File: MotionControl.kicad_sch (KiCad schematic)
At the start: 18 parts, among them J2 Conn_ARM_JTAG_SWD_10, Q1 2N7002, SW1 SW_Push, U1 ATSAMD21J18A-A, Y1 32.768kHz

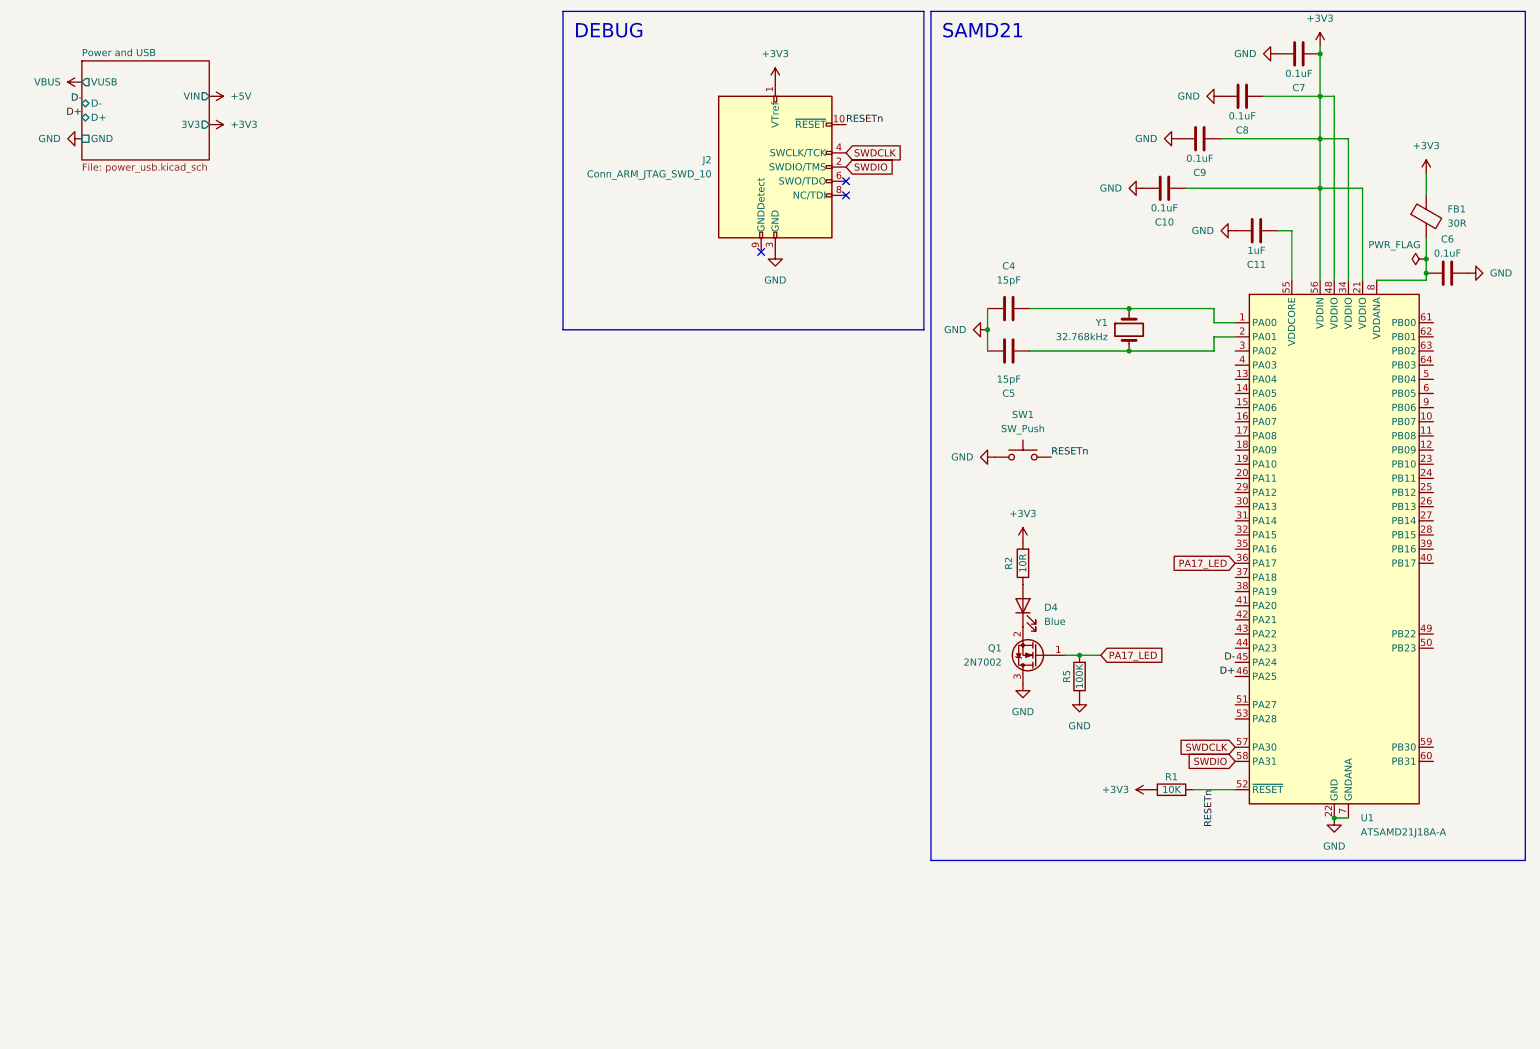
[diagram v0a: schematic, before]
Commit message: tx, rx leds
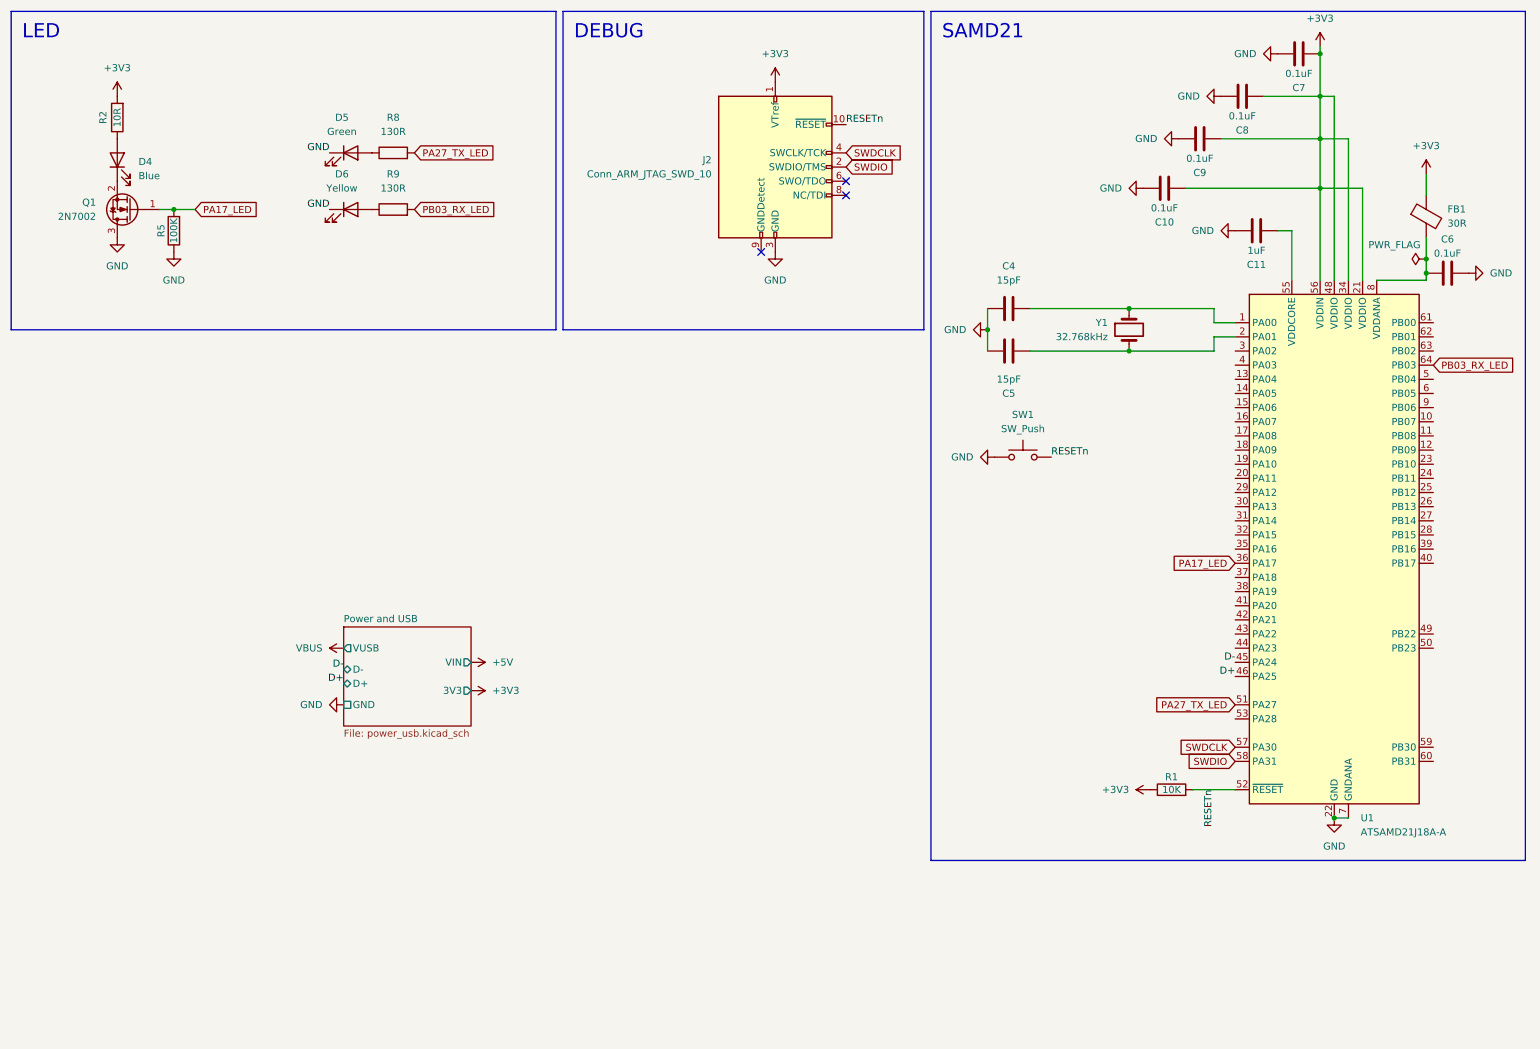
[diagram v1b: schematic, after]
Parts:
- added D5: Green, LED_SMD:LED_0603_1608Metric, symbol Device:LED
- added D6: Yellow, LED_SMD:LED_0603_1608Metric, symbol Device:LED
- added R8, R9: 130R, Resistor_SMD:R_0402_1005Metric, symbol Device:R
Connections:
- net GND: now also D5.1 (K), D6.1 (K)
- net PA27_TX_LED: now reaches U1.51 (PA27)
- net PA27_TX_LED: now also R8.2
- net PB03_RX_LED: now reaches U1.64 (PB03)
- net PB03_RX_LED: now also R9.2
- new net: D6.2 (A), R9.1
- new net: D5.2 (A), R8.1
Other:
- moved on the sheet: D4, Q1, R2, R5

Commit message: Stepper unit
Made first revision for stepper unit
Contains TMC5160, Status LED, FETs, and complementary comps
Will be x4 later
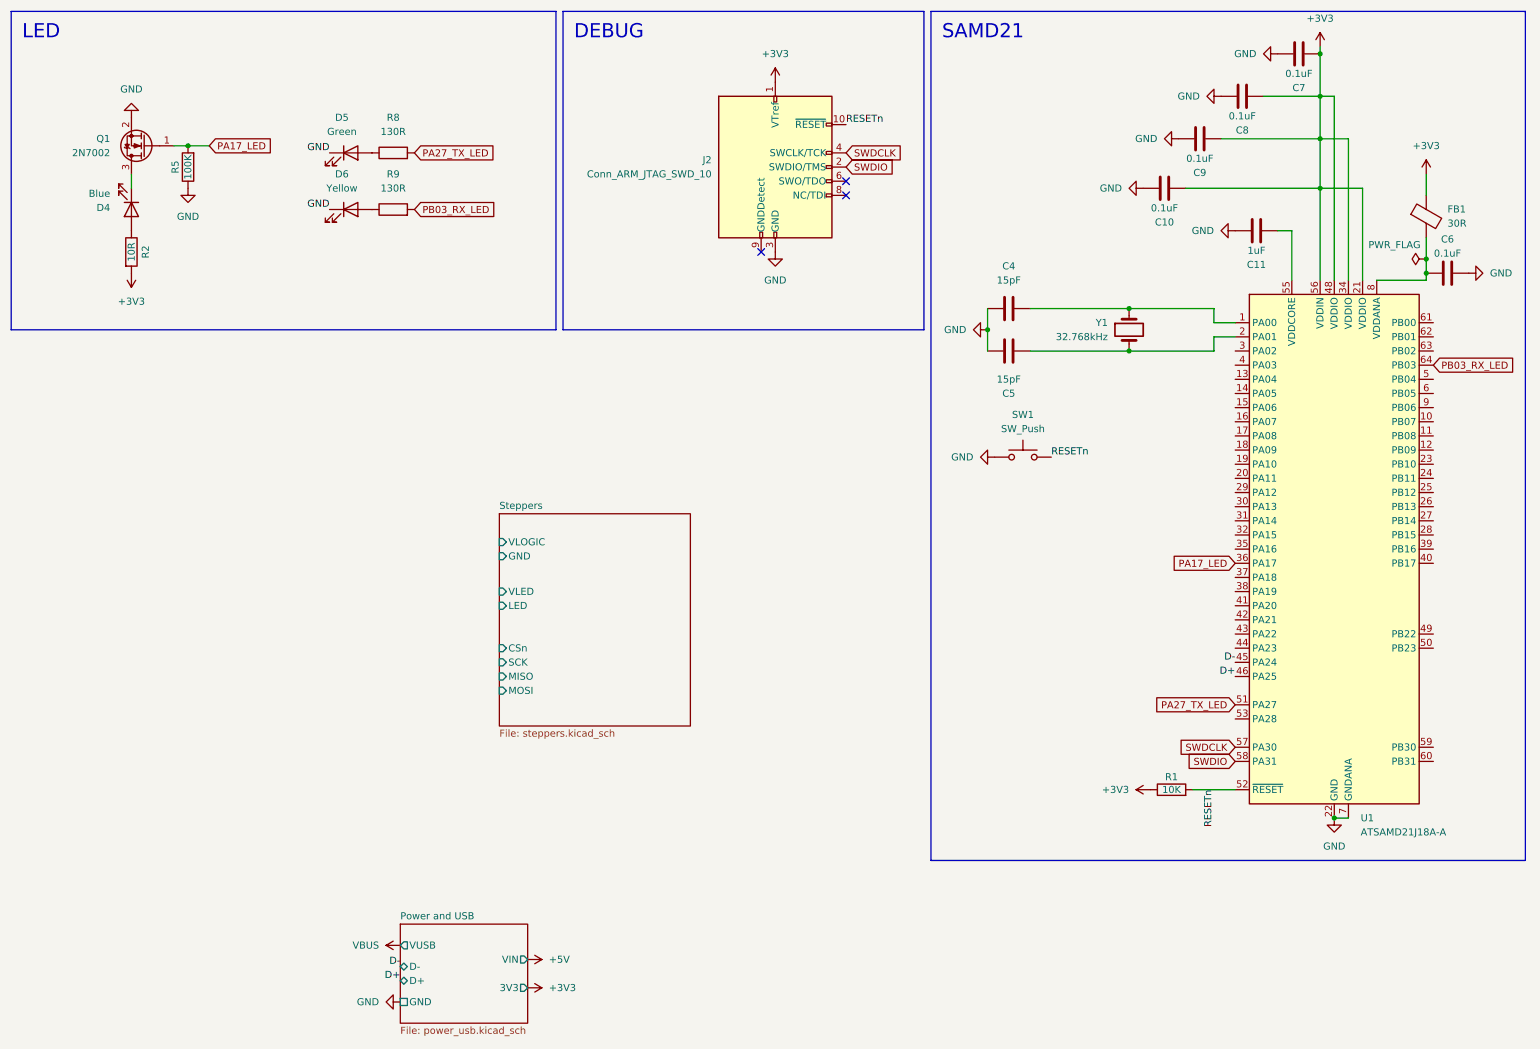
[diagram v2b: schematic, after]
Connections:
- net GND: now also Q1.2 (S); no longer Q1.3 (D)
- net at D4.1 (K): now also Q1.3 (D); no longer Q1.2 (S)
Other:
- added sheet Steppers (steppers.kicad_sch)
- moved on the sheet: Q1, R5

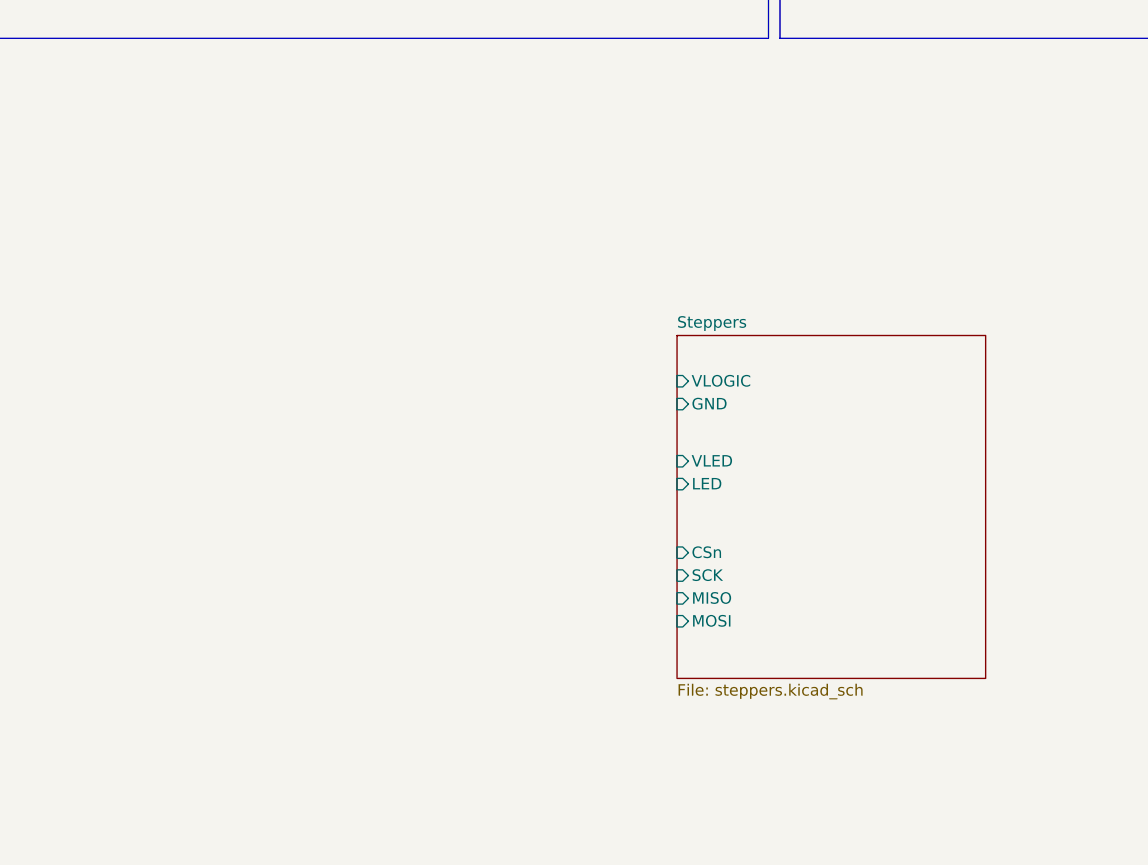
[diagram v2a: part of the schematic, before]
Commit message: x4 stepper units
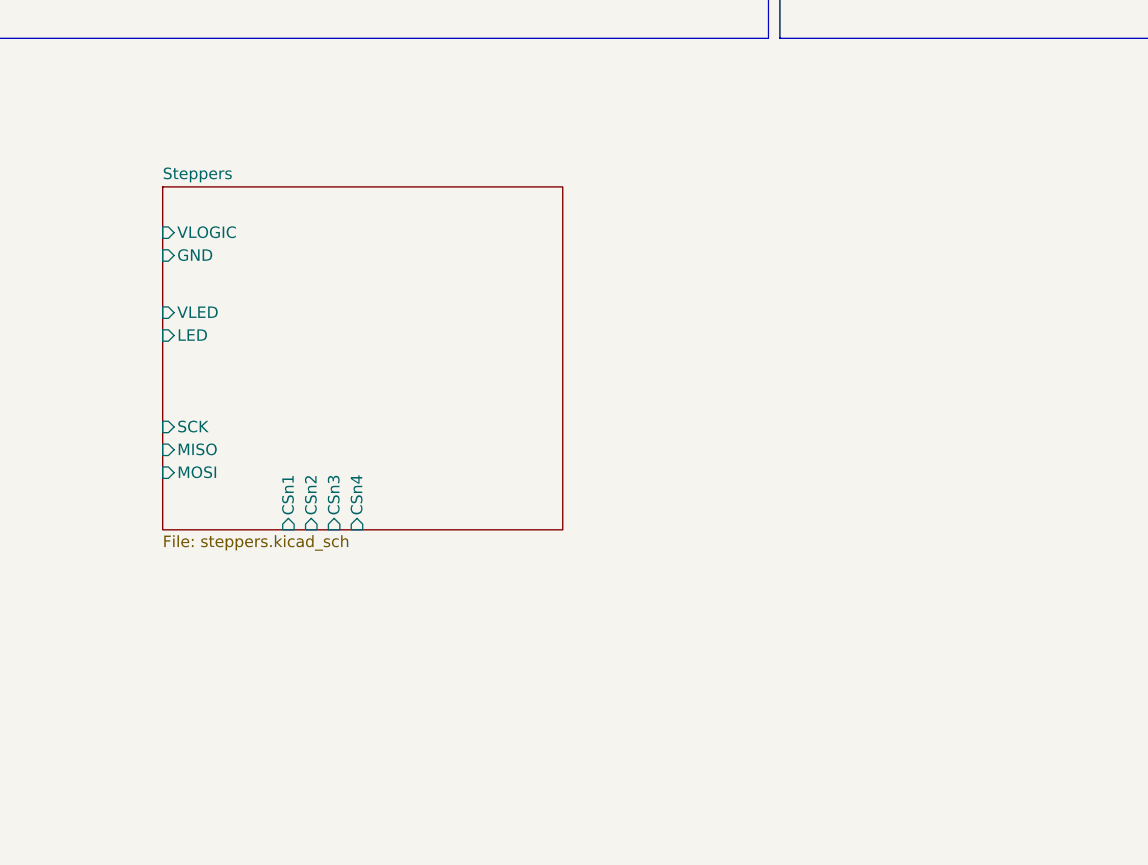
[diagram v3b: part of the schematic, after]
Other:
- sheet Steppers ports: added CSn1, CSn2, CSn3, CSn4; removed CSn
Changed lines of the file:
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@@
 	)
 	(sheet
-		(at 100.33 102.87)
-		(size 34.29 38.1)
+		(at 43.18 86.36)
+		(size 44.45 38.1)
 		(fields_autoplaced yes)
 		(stroke
@@
 		)
 		(property "Sheetname" "Steppers"
-			(at 100.33 102.1584 0)
+			(at 43.18 85.6484 0)
 			(effects
 				(font
@@
 		)
 		(property "Sheetfile" "steppers.kicad_sch"
-			(at 100.33 141.5546 0)
+			(at 43.18 125.0446 0)
 			(effects
 				(font
@@
 		)
 		(pin "VLOGIC" input
-			(at 100.33 107.95 180)
+			(at 43.18 91.44 180)
 			(effects
 				(font
@@
 		)
 		(pin "GND" input
-			(at 100.33 110.49 180)
+			(at 43.18 93.98 180)
 			(effects
 				(font
@@
 		)
 		(pin "LED" input
-			(at 100.33 119.38 180)
-			(effects
-				(font
-					(size 1.27 1.27)
-				)
-				(justify left)
-			)
-		)
-		(pin "CSn" input
-			(at 100.33 127 180)
+			(at 43.18 102.87 180)
 			(effects
 				(font
@@
 		)
 		(pin "SCK" input
-			(at 100.33 129.54 180)
+			(at 43.18 113.03 180)
 			(effects
 				(font
@@
 		)
 		(pin "VLED" input
-			(at 100.33 116.84 180)
+			(at 43.18 100.33 180)
 			(effects
 				(font
@@
 		)
 		(pin "MISO" input
-			(at 100.33 132.08 180)
+			(at 43.18 115.57 180)
 			(effects
 				(font
@@
 		)
 		(pin "MOSI" input
-			(at 100.33 134.62 180)
+			(at 43.18 118.11 180)
 			(effects
 				(font
+					(size 1.27 1.27)
+				)
+				(justify left)
+			)
+		)
+		(pin "CSn1" input
+			(at 57.15 124.46 270)
+			(effects
+				(font
+					(size 1.27 1.27)
+				)
+				(justify left)
+			)
+		)
+		(pin "CSn2" input
+			(at 59.69 124.46 270)
+			(effects
+				(font
+					(size 1.27 1.27)
+				)
+				(justify left)
+			)
+		)
+		(pin "CSn3" input
+			(at 62.23 124.46 270)
+			(effects
+				(font
+					(size 1.27 1.27)
+				)
+				(justify left)
+			)
+		)
+		(pin "CSn4" input
+			(at 64.77 124.46 270)
+			(effects
+				(font

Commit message: Lots of work
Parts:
- added C68: 0.1uF, Capacitor_SMD:C_0402_1005Metric, symbol Device:C
- added D11: WS2812B-2020, LED_SMD:LED_WS2812B-Mini_PLCC4_3.5x3.5mm, symbol LED:WS2812B
- added U7: TC4427, Package_SO:SOIC-8_3.9x4.9mm_P1.27mm, symbol Driver_FET2:TC4427
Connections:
- net +5V: now also C68.1, D11.1 (VDD), U7.6 (VDD)
- net GND: now also C68.2, D11.3 (VSS), U7.3 (GND)
- net Steppers/LED: now also D11.2 (DOUT)
- new net: D11.4 (DIN), U7.7 (OUTA)
- no-connect marks 3 -> 5

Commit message: lots of changes for mcu
more routed connections
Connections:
- net PA06_NEOPIX: now reaches U1.15 (PA06)
- net PA06_NEOPIX: now also U7.2 (INA)
- net PA16_LED: now reaches U1.35 (PA16)
- net PA16_LED: now also Q1.1 (G), R5.2
- removed net PA17_LED: Q1.1 (G), R5.2, U1.36 (PA17)
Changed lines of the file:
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@@
 		)
 	)
-	(global_label "PA17_LED"
+	(global_label "PA06_NEOPIX"
 		(shape input)
-		(at 232.41 111.76 180)
+		(at 60.96 102.87 180)
 		(fields_autoplaced yes)
 		(effects
@@
 		)
 		(property "Intersheetrefs" "${INTERSHEET_REFS}"
-			(at 220.2325 111.76 0)
+			(at 45.3353 102.87 0)
+			(effects
+				(font
+					(size 1.27 1.27)
+				)
+				(justify right)
+				(hide yes)
+			)
+		)
+	)
+	(global_label "PA16_LED"
+		(shape input)
+		(at 232.41 109.22 180)
+		(fields_autoplaced yes)
+		(effects
+			(font
+				(size 1.27 1.27)
+			)
+			(justify right)
+		)
+		(property "Intersheetrefs" "${INTERSHEET_REFS}"
+			(at 220.2325 109.22 0)
 			(effects
 				(font
@@
 		)
 	)
+	(global_label "PA16_LED"
+		(shape input)
+		(at 48.26 36.83 0)
+		(fields_autoplaced yes)
+		(effects
+			(font
+				(size 1.27 1.27)
+			)
+			(justify left)
+		)
+		(property "Intersheetrefs" "${INTERSHEET_REFS}"
+			(at 60.4375 36.83 0)
+			(effects
+				(font
+					(size 1.27 1.27)
+				)
+				(justify left)
+				(hide yes)
+			)
+		)
+	)
+	(global_label "PA06_NEOPIX"
+		(shape input)
+		(at 232.41 83.82 180)
+		(fields_autoplaced yes)
+		(effects
+			(font
+				(size 1.27 1.27)
+			)
+			(justify right)
+		)
+		(property "Intersheetrefs" "${INTERSHEET_REFS}"
+			(at 216.7853 83.82 0)
+			(effects
+				(font
+					(size 1.27 1.27)
+				)
+				(justify right)
+				(hide yes)
+			)
+		)
+	)
 	(global_label "PA27_TX_LED"
 		(shape input)
@@
 		)
 	)
-	(global_label "PA17_LED"
-		(shape input)
-		(at 48.26 36.83 0)
-		(fields_autoplaced yes)
-		(effects
-			(font
-				(size 1.27 1.27)
-			)
-			(justify left)
-		)
-		(property "Intersheetrefs" "${INTERSHEET_REFS}"
-			(at 60.4375 36.83 0)
-			(effects
-				(font
-					(size 1.27 1.27)
-				)
-				(justify left)
-				(hide yes)
-			)
-		)
-	)
 	(global_label "PB03_RX_LED"
 		(shape input)
@@
 		(on_board yes)
 		(dnp no)
-		(fields_autoplaced yes)
 		(property "Reference" "U7"
 			(at 69.85 93.98 0)
@@
 		)
 		(property "Footprint" "Package_SO:SOIC-8_3.9x4.9mm_P1.27mm"
-			(at 69.85 104.14 0)
+			(at 71.12 112.014 0)
 			(effects
 				(font
